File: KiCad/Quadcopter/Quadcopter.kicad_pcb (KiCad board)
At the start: 2 copper layers, 87.4 x 66.2 mm, 20 parts, among them J1 Conn_01x06, J2 Conn_01x03, J3 Conn_01x03, J4 Conn_01x04, J5 Conn_02x04_Odd_Even, J6 Conn_01x04, J7 Screw_Terminal_01x02, U1 BMP388, U2 ICM-20948_CJMCU, U3 Teensy4.1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

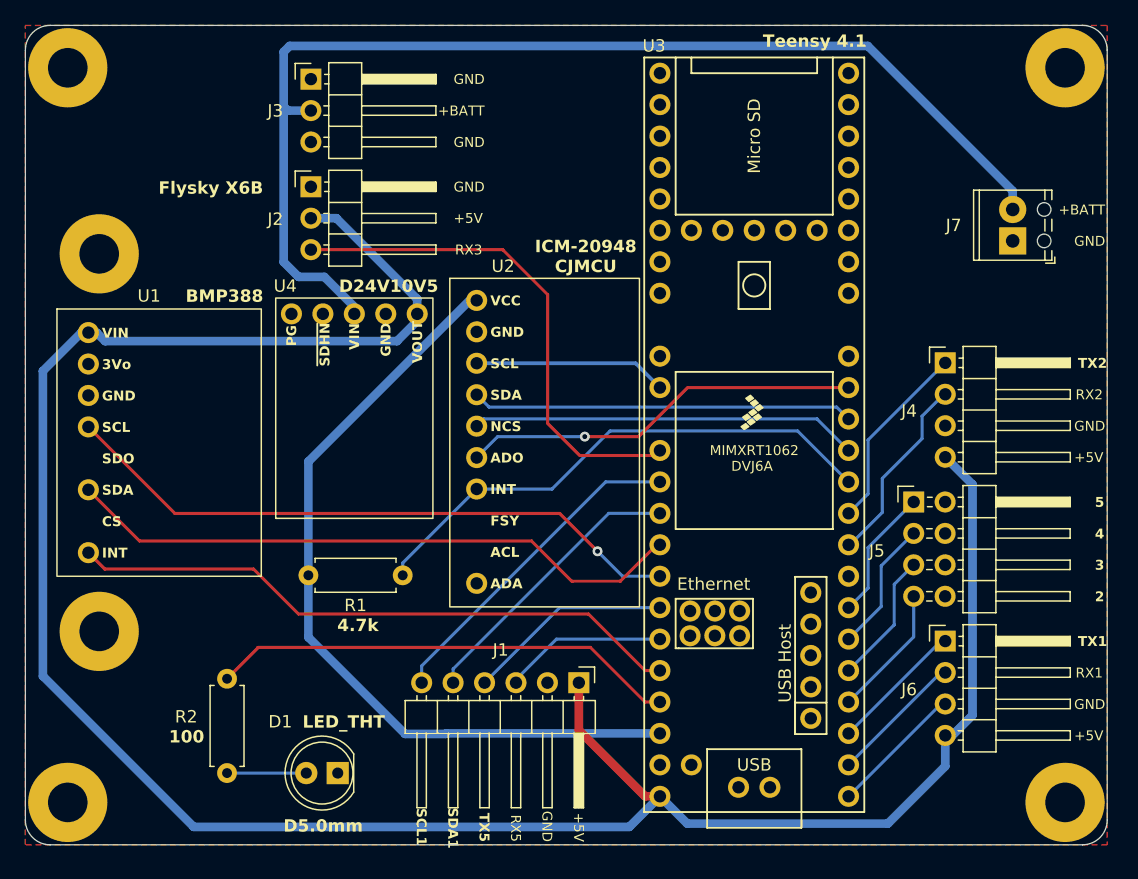
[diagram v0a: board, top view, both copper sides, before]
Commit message: - use screwless terminal block with side entry for power - use more generic pressure sensor name and more generic 5V DC-DC converter - add PCB name and date
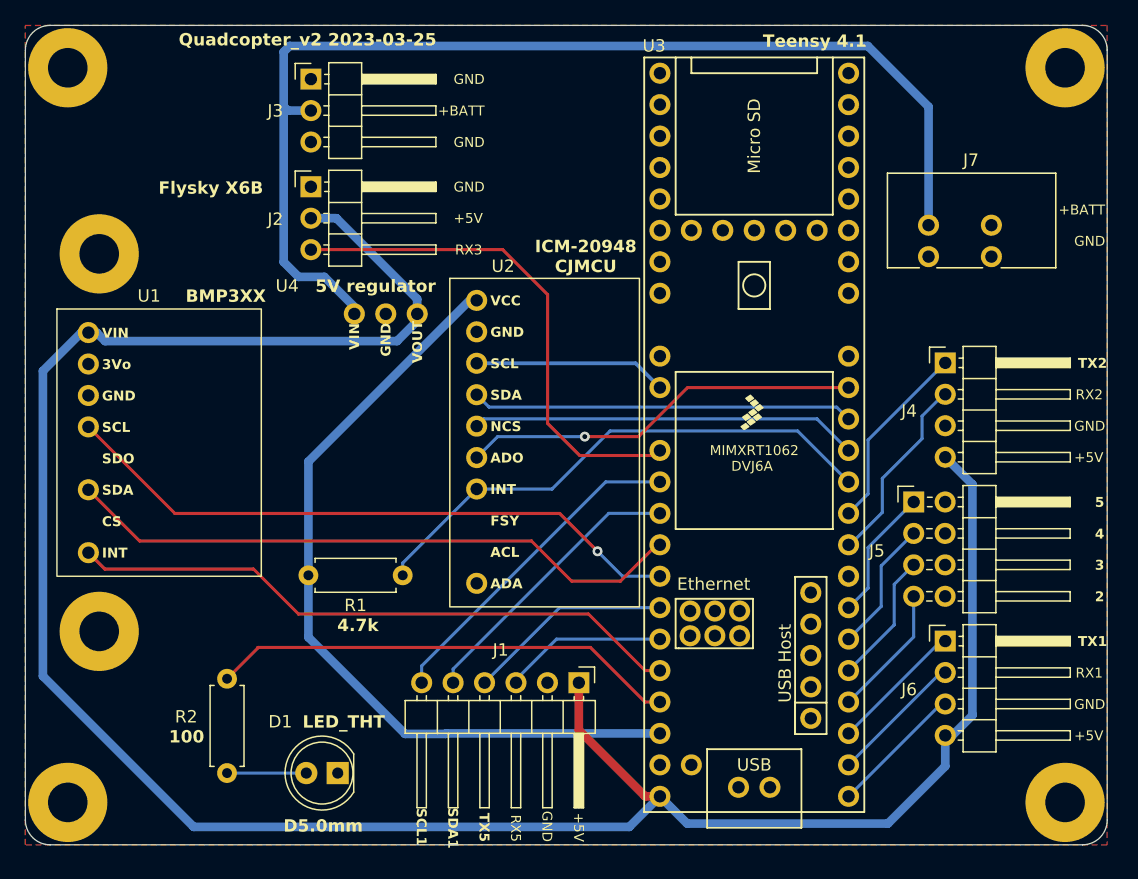
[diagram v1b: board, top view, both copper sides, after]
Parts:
- J7: value Screw_Terminal_01x02 -> Conn_01x02; footprint TerminalBlock_Phoenix:TerminalBlock_Phoenix_MPT-0,5-2-2.54_1x02_P2.54mm_Horizontal -> Quadcopter:691402910002B
- U4: value D24V10F5 -> DC-DC converter; footprint Lukas:D24V10F5 -> Lukas:DC-DC converter
- moved J7 4.26 mm to (176.9, 76.8)
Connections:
- J7 pad 1: GND -> +BATT
- J7 pad 2: +BATT -> GND
- U4 pad 1: unconnected-(U4-PG-Pad1) -> +BATT
- U4 pad 2: unconnected-(U4-~{SHDN}-Pad2) -> GND
- U4 pad 3: +BATT -> +5V
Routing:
- net +BATT: track 92.5 -> 91.0 mm
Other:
- board text added: "5V regulator"
- board text added: "BMP3XX"
- board text added: "Quadcopter_v2 2023-03-25"
- board text removed: "BMP388"
- board text removed: "D24V10V5"
- board text removed: "PG"
- board text removed: "~{SDHN}"
